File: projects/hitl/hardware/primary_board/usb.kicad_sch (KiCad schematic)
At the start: 31 parts, among them J1 USB-Micro-1981568-1, J5 CONN_01x02, Q2 SSM3K333R, U2 FT4222H, Y1 Crystal_12MHz

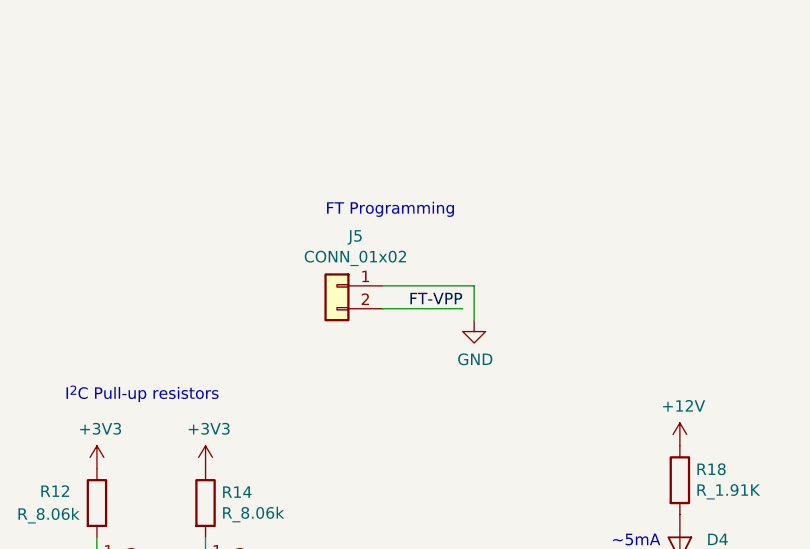
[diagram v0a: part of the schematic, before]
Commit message: Switch FTPROG to button and update I2C level shifter
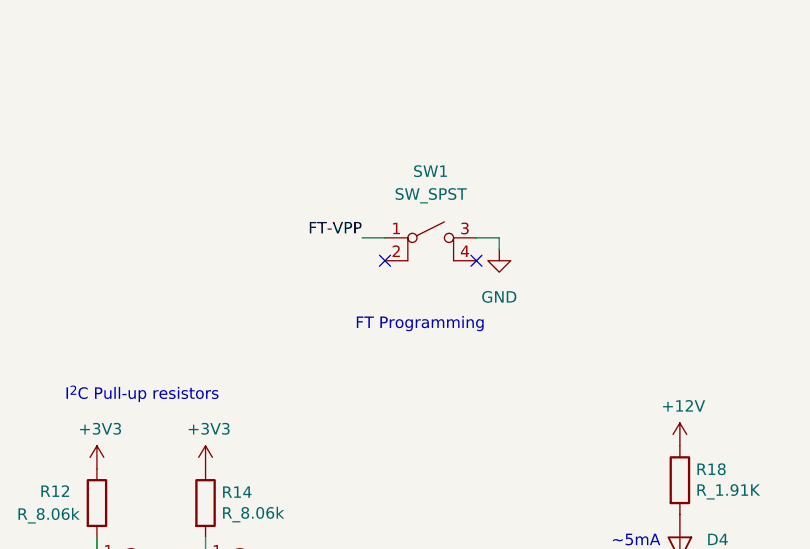
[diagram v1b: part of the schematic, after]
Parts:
- removed J5: CONN_01x02, footprints:pinheader_1x2, symbol formula:CONN_01x02
- added SW1: SW_SPST, footprints:Button_PTS526, symbol formula:SW_SPST
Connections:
- net FT-VPP: now also SW1.1 (A)
- net GND: now also SW1.3 (B)
- no-connect marks 8 -> 10
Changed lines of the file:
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@@
   (no_connect (at 167.64 81.28))
   (no_connect (at 148.59 74.93))
+  (no_connect (at 223.774 54.356))
   (no_connect (at 167.64 106.68))
   (no_connect (at 167.64 104.14))
+  (no_connect (at 213.614 54.356))
   (no_connect (at 167.64 86.36))
   (no_connect (at 167.64 111.76))
@@
     (stroke (width 0) (type default) (color 0 0 0 0))
   )
-  (wire (pts (xy 222.25 59.69) (xy 213.36 59.69))
-    (stroke (width 0) (type default) (color 0 0 0 0))
-  )
   (wire (pts (xy 90.932 183.388) (xy 90.932 185.928))
     (stroke (width 0) (type default) (color 0 0 0 0))
@@
     (stroke (width 0) (type default) (color 0 0 0 0))
   )
-  (wire (pts (xy 223.52 57.15) (xy 213.36 57.15))
-    (stroke (width 0) (type default) (color 0 0 0 0))
-  )
   (wire (pts (xy 105.41 119.38) (xy 99.06 119.38))
     (stroke (width 0) (type default) (color 0 0 0 0))
@@
     (stroke (width 0) (type default) (color 0 0 0 0))
   )
+  (wire (pts (xy 223.774 51.816) (xy 226.314 51.816))
+    (stroke (width 0) (type default) (color 0 0 0 0))
+  )
   (wire (pts (xy 59.182 184.658) (xy 59.182 187.198))
     (stroke (width 0) (type default) (color 0 0 0 0))
@@
     (stroke (width 0) (type default) (color 0 0 0 0))
   )
+  (wire (pts (xy 226.314 51.816) (xy 226.314 53.086))
+    (stroke (width 0) (type default) (color 0 0 0 0))
+  )
   (wire (pts (xy 65.532 184.658) (xy 65.532 187.198))
     (stroke (width 0) (type default) (color 0 0 0 0))
@@
     (stroke (width 0) (type default) (color 0 0 0 0))
   )
-  (wire (pts (xy 223.52 60.96) (xy 223.52 57.15))
-    (stroke (width 0) (type default) (color 0 0 0 0))
-  )
   (wire (pts (xy 102.87 102.87) (xy 101.6 102.87))
     (stroke (width 0) (type default) (color 0 0 0 0))
@@
   )
   (wire (pts (xy 193.675 87.63) (xy 193.675 85.09))
+    (stroke (width 0) (type default) (color 0 0 0 0))
+  )
+  (wire (pts (xy 211.074 51.816) (xy 213.614 51.816))
     (stroke (width 0) (type default) (color 0 0 0 0))
   )
@@
     (effects (font (size 1.27 1.27)) (justify left bottom))
   )
-  (text "FT Programming" (at 207.01 49.53 0)
+  (text "FT Programming" (at 210.312 62.23 0)
     (effects (font (size 1.27 1.27)) (justify left bottom))
   )
@@
     (effects (font (size 1.27 1.27)) (justify right bottom))
   )
-  (label "FT-VPP" (at 222.25 59.69 180)
+  (label "FT-VPP" (at 211.074 51.816 180)
     (effects (font (size 1.27 1.27)) (justify right bottom))
   )
@@
     (pin "1")
   )
-  (symbol (lib_id "power:GND") (at 223.52 60.96 0) (unit 1)
-    (in_bom yes) (on_board yes)
-    (property "Reference" "#PWR?" (id 0) (at 223.52 67.31 0)
-      (effects (font (size 1.27 1.27)) hide)
-    )
-    (property "Value" "GND" (id 1) (at 223.647 65.3542 0))
-    (property "Footprint" "" (id 2) (at 223.52 60.96 0)
-      (effects (font (size 1.27 1.27)) hide)
-    )
-    (property "Datasheet" "" (id 3) (at 223.52 60.96 0)
-      (effects (font (size 1.27 1.27)) hide)
-    )
-    (pin "1")
-  )
   (symbol (lib_id "power:+5V") (at 127.762 169.672 0) (unit 1)
     (in_bom yes) (on_board yes)
@@
     (pin "2")
   )
+  (symbol (lib_id "power:GND") (at 226.314 53.086 0) (unit 1)
+    (in_bom yes) (on_board yes) (fields_autoplaced)
+    (property "Reference" "#PWR?" (id 0) (at 226.314 59.436 0)
+      (effects (font (size 1.27 1.27)) hide)
+    )
+    (property "Value" "GND" (id 1) (at 226.314 58.42 0))
+    (property "Footprint" "" (id 2) (at 226.314 53.086 0)
+      (effects (font (size 1.27 1.27)) hide)
+    )
+    (property "Datasheet" "" (id 3) (at 226.314 53.086 0)
+      (effects (font (size 1.27 1.27)) hide)
+    )
+    (pin "1")
+  )
   (symbol (lib_id "power:GND") (at 99.06 147.32 0) (unit 1)
     (in_bom yes) (on_board yes)
@@
     )
     (pin "1")
+  )
+  (symbol (lib_id "formula:SW_SPST") (at 218.694 51.816 0) (unit 1)
+    (in_bom yes) (on_board yes) (fields_autoplaced)
+    (property "Reference" "SW1" (id 0) (at 218.694 44.45 0))
+    (property "Value" "SW_SPST" (id 1) (at 218.694 46.99 0))
+    (property "Footprint" "footprints:Button_PTS526" (id 2) (at 218.694 51.816 0)
+      (effects (font (size 1.27 1.27)) hide)
+    )
+    (property "Datasheet" "~" (id 3) (at 218.694 51.816 0)
+      (effects (font (size 1.27 1.27)) hide)
+    )
+    (property "DigikeyLink" "https://www.digikey.com/en/products/detail/c-k/PTS526-SK15-SMTR2-LFS/10056626" (id 4) (at 218.694 51.816 0)
+      (effects (font (size 1.27 1.27)) hide)
+    )
+    (property "DigikeyPartNumber" "CKN12221-1-ND" (id 5) (at 218.694 51.816 0)
+      (effects (font (size 1.27 1.27)) hide)
+    )
+    (property "MPN" "PTS526 SK15 SMTR2 LFS" (id 6) (at 218.694 51.816 0)
+      (effects (font (size 1.27 1.27)) hide)
+    )
+    (pin "2")
+    (pin "4")
+    (pin "1")
+    (pin "3")
   )
   (symbol (lib_id "power:GND") (at 45.466 104.14 0) (unit 1)
@@
     )
     (pin "1")
-    (pin "2")
-  )
-  (symbol (lib_id "formula:CONN_01x02") (at 208.28 57.15 0) (mirror y) (unit 1)
-    (in_bom yes) (on_board yes)
-    (property "Reference" "J5" (id 0) (at 210.3628 51.6382 0))
-    (property "Value" "CONN_01x02" (id 1) (at 210.3628 53.9496 0))
-    (property "Footprint" "footprints:pinheader_1x2" (id 2) (at 210.82 57.15 0)
-      (effects (font (size 1.27 1.27)) hide)
-    )
-    (property "Datasheet" "https://katalog.we-online.de/em/datasheet/6130xx11121.pdf" (id 3) (at 208.28 54.61 0)
-      (effects (font (size 1.27 1.27)) hide)
-    )
-    (property "MFN" "DK" (id 4) (at 205.74 52.07 0)
-      (effects (font (size 1.27 1.27)) hide)
-    )
-    (property "MPN" "732-5315-ND" (id 5) (at 203.2 49.53 0)
-      (effects (font (size 1.27 1.27)) hide)
-    )
-    (pin "1")
